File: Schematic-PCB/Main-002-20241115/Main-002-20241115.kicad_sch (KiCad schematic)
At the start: 88 parts, among them J1 Conn_PWR, J10 Conn_UI, J2 Conn_NeoPixel, J3 Conn_NeoPixel, J4 Conn_NeoPixel, J5 CamS3-6, J6 CamS3-4, J7 Pixy 2.1, J8 Conn_MD, J9 Conn_Dribbler, SW1 SW_DPDT_x2, SW2 Main_RST, SW3 Cam_RST, SW4 Cam_RST, U1 DEV-16771, U10 TSSP4038, U11 TSSP4038, U12 TSSP4038, U13 TSSP4038, U14 TSSP4038, U15 TSSP4038, U16 TSSP4038, U17 TSSP4038, U18 TSSP4038, U3 TSSP4038, U4 TSSP4038, U5 TSSP4038, U6 TSSP4038, U7 TSSP4038, U8 TSSP4038, U9 TSSP4038

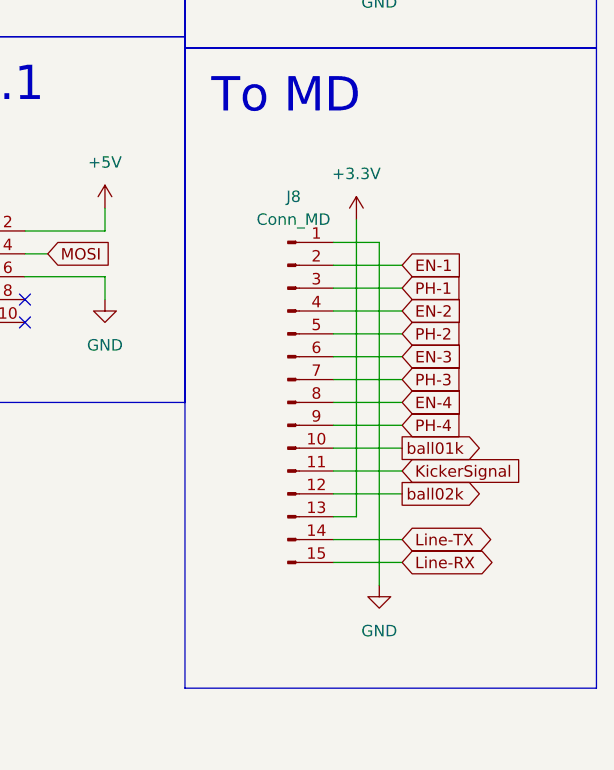
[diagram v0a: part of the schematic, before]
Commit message: update: メイン基板を開いたりしてピンアサインを確認した
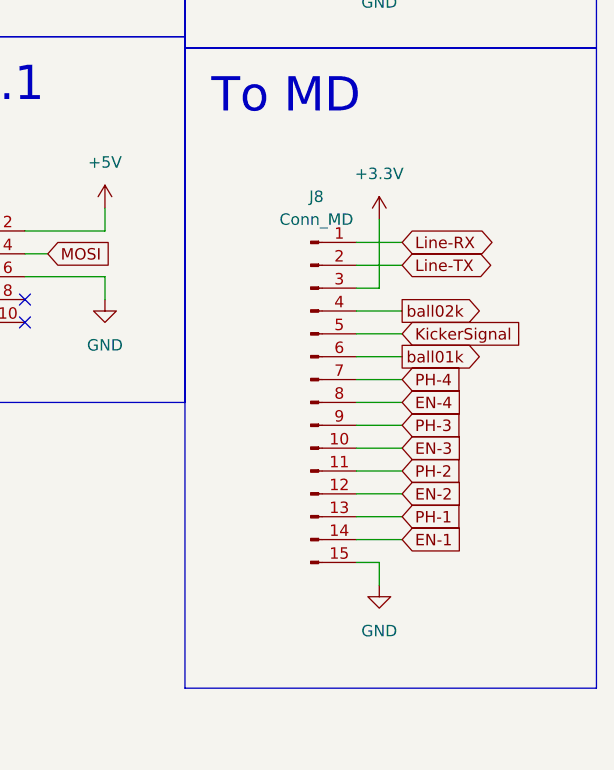
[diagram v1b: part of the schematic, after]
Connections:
- net +3.3V: now also J8.3 (Pin_3); no longer J8.13 (Pin_13)
- net EN-1: now also J8.14 (Pin_14); no longer J8.2 (Pin_2)
- net EN-2: now also J8.12 (Pin_12); no longer J8.4 (Pin_4)
- net EN-3: now also J8.10 (Pin_10); no longer J8.6 (Pin_6)
- net GND: now also J8.15 (Pin_15); no longer J8.1 (Pin_1)
- net KickerSignal: now also J8.5 (Pin_5); no longer J8.11 (Pin_11)
- net Line-RX: now also J8.1 (Pin_1); no longer J8.15 (Pin_15)
- net Line-TX: now also J8.2 (Pin_2); no longer J8.14 (Pin_14)
- net PH-1: now also J8.13 (Pin_13); no longer J8.3 (Pin_3)
- net PH-2: now also J8.11 (Pin_11); no longer J8.5 (Pin_5)
- net PH-3: now also J8.9 (Pin_9); no longer J8.7 (Pin_7)
- net PH-4: now also J8.7 (Pin_7); no longer J8.9 (Pin_9)
- net ball01k: now also J8.6 (Pin_6); no longer J8.10 (Pin_10)
- net ball02k: now also J8.4 (Pin_4); no longer J8.12 (Pin_12)
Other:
- moved on the sheet: J8
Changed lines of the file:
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@@
 	(wire
 		(pts
-			(xy 560.07 144.78) (xy 552.45 144.78)
+			(xy 560.07 154.94) (xy 554.99 154.94)
 		)
 		(stroke
@@
 	(wire
 		(pts
-			(xy 560.07 137.16) (xy 552.45 137.16)
+			(xy 560.07 162.56) (xy 554.99 162.56)
 		)
 		(stroke
@@
 	(wire
 		(pts
-			(xy 554.99 129.54) (xy 554.99 162.56)
+			(xy 557.53 129.54) (xy 557.53 137.16)
 		)
 		(stroke
@@
 	(wire
 		(pts
-			(xy 557.53 132.08) (xy 557.53 170.18)
+			(xy 557.53 167.64) (xy 557.53 170.18)
 		)
 		(stroke
@@
 	(wire
 		(pts
-			(xy 552.45 162.56) (xy 554.99 162.56)
+			(xy 554.99 137.16) (xy 557.53 137.16)
 		)
 		(stroke
@@
 	(wire
 		(pts
-			(xy 552.45 160.02) (xy 560.07 160.02)
+			(xy 554.99 139.7) (xy 560.07 139.7)
 		)
 		(stroke
@@
 	(wire
 		(pts
-			(xy 552.45 154.94) (xy 560.07 154.94)
+			(xy 554.99 144.78) (xy 560.07 144.78)
 		)
 		(stroke
@@
 	(wire
 		(pts
-			(xy 552.45 167.64) (xy 560.07 167.64)
+			(xy 554.99 132.08) (xy 560.07 132.08)
 		)
 		(stroke
@@
 	(wire
 		(pts
-			(xy 560.07 149.86) (xy 552.45 149.86)
+			(xy 560.07 149.86) (xy 554.99 149.86)
 		)
 		(stroke
@@
 	(wire
 		(pts
-			(xy 552.45 132.08) (xy 557.53 132.08)
+			(xy 554.99 167.64) (xy 557.53 167.64)
 		)
 		(stroke
@@
 	(wire
 		(pts
-			(xy 560.07 139.7) (xy 552.45 139.7)
+			(xy 560.07 160.02) (xy 554.99 160.02)
 		)
 		(stroke
@@
 	(wire
 		(pts
-			(xy 560.07 142.24) (xy 552.45 142.24)
+			(xy 560.07 157.48) (xy 554.99 157.48)
 		)
 		(stroke
@@
 	(wire
 		(pts
-			(xy 560.07 147.32) (xy 552.45 147.32)
+			(xy 560.07 152.4) (xy 554.99 152.4)
 		)
 		(stroke
@@
 	(wire
 		(pts
-			(xy 552.45 165.1) (xy 560.07 165.1)
+			(xy 554.99 134.62) (xy 560.07 134.62)
 		)
 		(stroke
@@
 	(wire
 		(pts
-			(xy 560.07 134.62) (xy 552.45 134.62)
+			(xy 560.07 165.1) (xy 554.99 165.1)
 		)
 		(stroke
@@
 	(wire
 		(pts
-			(xy 552.45 157.48) (xy 560.07 157.48)
+			(xy 554.99 142.24) (xy 560.07 142.24)
 		)
 		(stroke
@@
 	(wire
 		(pts
-			(xy 560.07 152.4) (xy 552.45 152.4)
+			(xy 560.07 147.32) (xy 554.99 147.32)
 		)
 		(stroke
@@
 	(global_label "ball01k"
 		(shape output)
-		(at 560.07 154.94 0)
+		(at 560.07 144.78 0)
 		(fields_autoplaced yes)
 		(effects
@@
 		)
 		(property "Intersheetrefs" "${INTERSHEET_REFS}"
-			(at 570.1307 154.94 0)
+			(at 570.1307 144.78 0)
 			(effects
 				(font
@@
 	(global_label "PH-1"
 		(shape input)
-		(at 560.07 137.16 0)
+		(at 560.07 162.56 0)
 		(fields_autoplaced yes)
 		(effects
@@
 		)
 		(property "Intersheetrefs" "${INTERSHEET_REFS}"
-			(at 568.4376 137.16 0)
+			(at 568.4376 162.56 0)
 			(effects
 				(font
@@
 	(global_label "Line-RX"
 		(shape bidirectional)
-		(at 560.07 167.64 0)
+		(at 560.07 132.08 0)
 		(fields_autoplaced yes)
 		(effects
@@
 		)
 		(property "Intersheetrefs" "${INTERSHEET_REFS}"
-			(at 585.9756 167.64 0)
+			(at 585.9756 132.08 0)
 			(effects
 				(font
@@
 	(global_label "EN-1"
 		(shape input)
-		(at 560.07 134.62 0)
+		(at 560.07 165.1 0)
 		(fields_autoplaced yes)
 		(effects
@@
 		)
 		(property "Intersheetrefs" "${INTERSHEET_REFS}"
-			(at 568.3166 134.62 0)
+			(at 568.3166 165.1 0)
 			(effects
 				(font
@@
 	(global_label "KickerSignal"
 		(shape input)
-		(at 560.07 157.48 0)
+		(at 560.07 142.24 0)
 		(fields_autoplaced yes)
 		(effects
@@
 		)
 		(property "Intersheetrefs" "${INTERSHEET_REFS}"
-			(at 574.848 157.48 0)
+			(at 574.848 142.24 0)
 			(effects
 				(font
@@
 	(global_label "PH-4"
 		(shape input)
-		(at 560.07 152.4 0)
+		(at 560.07 147.32 0)
 		(fields_autoplaced yes)
 		(effects
@@
 		)
 		(property "Intersheetrefs" "${INTERSHEET_REFS}"
-			(at 568.4376 152.4 0)
+			(at 568.4376 147.32 0)
 			(effects
 				(font
@@
 	(global_label "Line-TX"
 		(shape bidirectional)
-		(at 560.07 165.1 0)
+		(at 560.07 134.62 0)
 		(fields_autoplaced yes)
 		(effects
@@
 		)
 		(property "Intersheetrefs" "${INTERSHEET_REFS}"
-			(at 586.278 165.1 0)
+			(at 586.278 134.62 0)
 			(effects
 				(font
@@
 	(global_label "EN-3"
 		(shape input)
-		(at 560.07 144.78 0)
+		(at 560.07 154.94 0)
 		(fields_autoplaced yes)
 		(effects
@@
 		)
 		(property "Intersheetrefs" "${INTERSHEET_REFS}"
-			(at 568.3166 144.78 0)
+			(at 568.3166 154.94 0)
 			(effects
 				(font
@@
 	(global_label "PH-2"
 		(shape input)
-		(at 560.07 142.24 0)
+		(at 560.07 157.48 0)
 		(fields_autoplaced yes)
 		(effects
@@
 		)
 		(property "Intersheetrefs" "${INTERSHEET_REFS}"
-			(at 568.4376 142.24 0)
+			(at 568.4376 157.48 0)
 			(effects
 				(font
@@
 	(global_label "ball02k"
 		(shape output)
-		(at 560.07 160.02 0)
+		(at 560.07 139.7 0)
 		(fields_autoplaced yes)
 		(effects
@@
 		)
 		(property "Intersheetrefs" "${INTERSHEET_REFS}"
-			(at 570.1307 160.02 0)
+			(at 570.1307 139.7 0)
 			(effects
 				(font
@@
 	(global_label "PH-3"
 		(shape input)
-		(at 560.07 147.32 0)
+		(at 560.07 152.4 0)
 		(fields_autoplaced yes)
 		(effects
@@
 		)
 		(property "Intersheetrefs" "${INTERSHEET_REFS}"
-			(at 568.4376 147.32 0)
+			(at 568.4376 152.4 0)
 			(effects
 				(font
@@
 	(global_label "EN-2"
 		(shape input)
-		(at 560.07 139.7 0)
+		(at 560.07 160.02 0)
 		(fields_autoplaced yes)
 		(effects
@@
 		)
 		(property "Intersheetrefs" "${INTERSHEET_REFS}"
-			(at 568.3166 139.7 0)
+			(at 568.3166 160.02 0)
 			(effects
 				(font
@@
 	(symbol
 		(lib_id "power:+3.3V")
-		(at 554.99 129.54 0)
+		(at 557.53 129.54 0)
+		(mirror y)
 		(unit 1)
 		(exclude_from_sim no)
@@
 		(fields_autoplaced yes)
 		(property "Reference" "#PWR041"
-			(at 554.99 133.35 0)
+			(at 557.53 133.35 0)
 			(effects
 				(font
@@
 		)
 		(property "Value" "+3.3V"
-			(at 554.99 124.46 0)
+			(at 557.53 124.46 0)
 			(effects
 				(font
@@
 		)
 		(property "Footprint" ""
-			(at 554.99 129.54 0)
+			(at 557.53 129.54 0)
 			(effects
 				(font
@@
 		)
 		(property "Datasheet" ""
-			(at 554.99 129.54 0)
+			(at 557.53 129.54 0)
 			(effects
 				(font
@@
 		)
 		(property "Description" "Power symbol creates a global label with name \"+3.3V\""
-			(at 554.99 129.54 0)
+			(at 557.53 129.54 0)
 			(effects
 				(font
@@
 	(symbol
 		(lib_id "Connector:Conn_01x15_Pin")
-		(at 547.37 149.86 0)
+		(at 549.91 149.86 0)
 		(unit 1)
 		(exclude_from_sim no)
@@
 		(dnp no)
 		(property "Reference" "J8"
-			(at 548.005 127 0)
+			(at 550.545 127 0)
 			(effects
 				(font
@@
 		)
 		(property "Value" "Conn_MD"
-			(at 548.005 129.54 0)
+			(at 550.545 129.54 0)
 			(effects
 				(font
@@
 		)
 		(property "Footprint" "@2024TOINIOT2-MD:1.0K-FX-15PWB"
-			(at 547.37 149.86 0)
+			(at 549.91 149.86 0)
 			(effects
 				(font
@@
 		)
 		(property "Datasheet" "~"
-			(at 547.37 149.86 0)
+			(at 549.91 149.86 0)
 			(effects
 				(font
@@
 		)
 		(property "Description" "Generic connector, single row, 01x15, script generated"
-			(at 547.37 149.86 0)
+			(at 549.91 149.86 0)
 			(effects
 				(font
@@
 		(lib_id "power:GND")
 		(at 557.53 170.18 0)
+		(mirror y)
 		(unit 1)
 		(exclude_from_sim no)
